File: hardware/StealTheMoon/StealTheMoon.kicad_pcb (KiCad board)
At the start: 2 copper layers, 21 parts, among them J1 Motor, J2 Motor, J3 Servo, J4 Servo, J5 Conn_01x10, J6 BAT, U1 ESP32-DEVKIT-V1, U2 ROB-14450, U3 L7805CV, U4 L7805CV

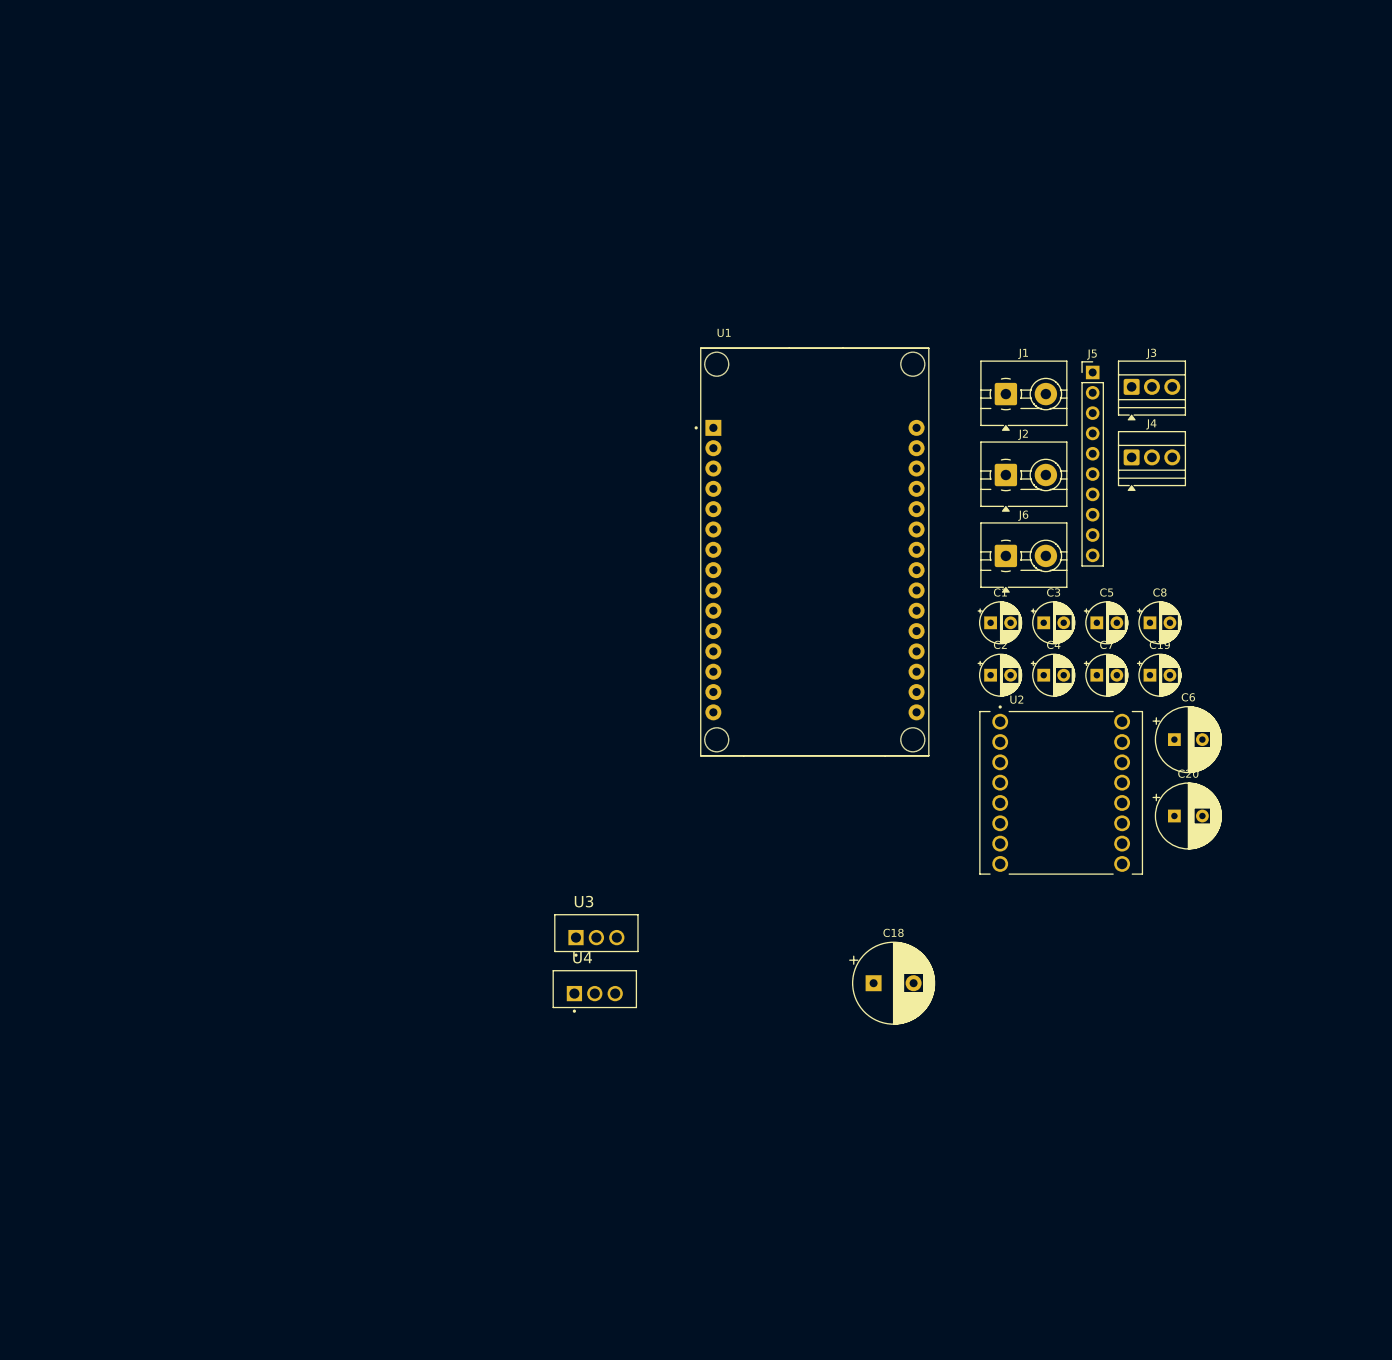
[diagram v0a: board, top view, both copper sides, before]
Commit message: Finish layout and generate gbr files for fabrication
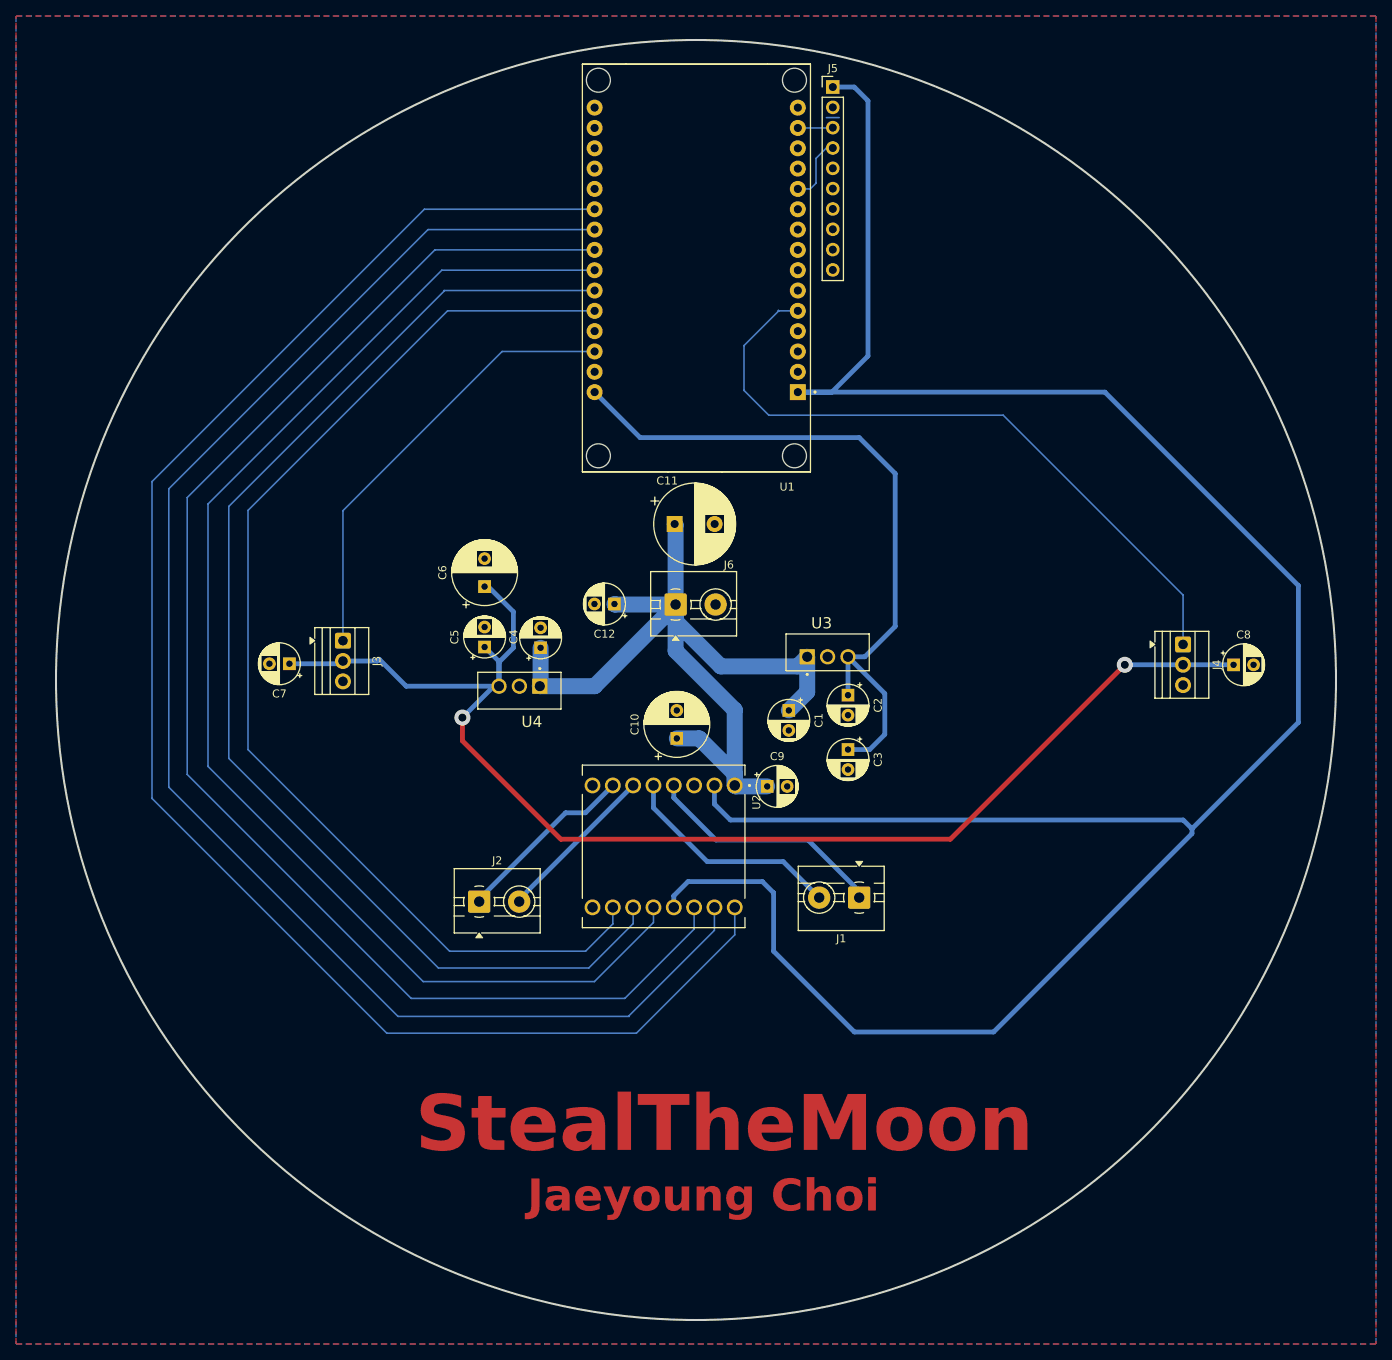
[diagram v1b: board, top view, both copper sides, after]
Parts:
- added C9: 100n, Capacitor_THT:CP_Radial_D5.0mm_P2.50mm, F.Cu at (112.9, 112.3)
- moved J3 103.6 mm to (59.9, 94.1), turned to -90 degrees
- moved C7 100.9 mm to (53.2, 97.0), turned to 180 degrees
- moved C6 88.3 mm to (77.6, 87.3), turned to 90 degrees
- moved J2 84.7 mm to (76.9, 126.7)
- moved C5 76.6 mm to (77.6, 94.9), turned to 90 degrees
- moved C12 67.5 mm to (93.8, 89.5), turned to 180 degrees
- moved J1 65.6 mm to (124.4, 126.2), turned to 180 degrees
- moved C4 63.0 mm to (84.6, 95.0), turned to 90 degrees
- moved C10 63.0 mm to (101.6, 106.3), turned to 90 degrees
- moved C11 62.6 mm to (101.3, 79.5)
- moved U2 50.1 mm to (100.0, 119.8), turned to -90 degrees
- moved J5 48.3 mm to (121.1, 24.9)
- moved U3 45.5 mm to (117.9, 96.1)
- moved J6 41.7 mm to (101.5, 89.6)
- moved U4 38.7 mm to (84.5, 99.8), turned to 180 degrees
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- renumbered C20 to C10, C18 to C11, C19 to C12
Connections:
- U1 pad 21: /PWMB -> /PWMA
- U1 pad 22: /BI1 -> /AI2
- U1 pad 23: /AI2 -> /AI1
- U1 pad 24: /AI1 -> /BI1
- U1 pad 25: /PWMA -> /BI2
- U1 pad 26: /BI2 -> /PWMB
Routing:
- net 3.3V: track 0.00 -> 309.3 mm
- net /PWMA: track 0.00 -> 202.6 mm
- net /AI2: track 0.00 -> 191.5 mm
- net /AI1: track 0.00 -> 179.6 mm
- net 5V2: track 0.00 -> 168.2 mm, vias 0 -> 2
- net /BI1: track 0.00 -> 165.0 mm
- net /BI2: track 0.00 -> 154.2 mm
- net /PWMB: track 0.00 -> 143.1 mm
- net 9V: track 0.00 -> 113.2 mm
- net 5V1: track 0.00 -> 90.8 mm
- net /Sv2: track 0.00 -> 85.9 mm
- net /Sv1: track 0.00 -> 56.0 mm
- net Net-(J1-Pin_1): track 0.00 -> 30.4 mm
- net Net-(J1-Pin_2): track 0.00 -> 28.2 mm
- net Net-(J2-Pin_1): track 0.00 -> 22.9 mm
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- added copper zone on B.Cu, net GND
- added copper zone on F.Cu, net GND
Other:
- board outline added: 160 x 160 mm
- copper layers 2 -> 4
- board text added: "Jaeyoung Choi"
- board text added: "StealTheMoon"

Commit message: Reroute the PCB to make it smaller
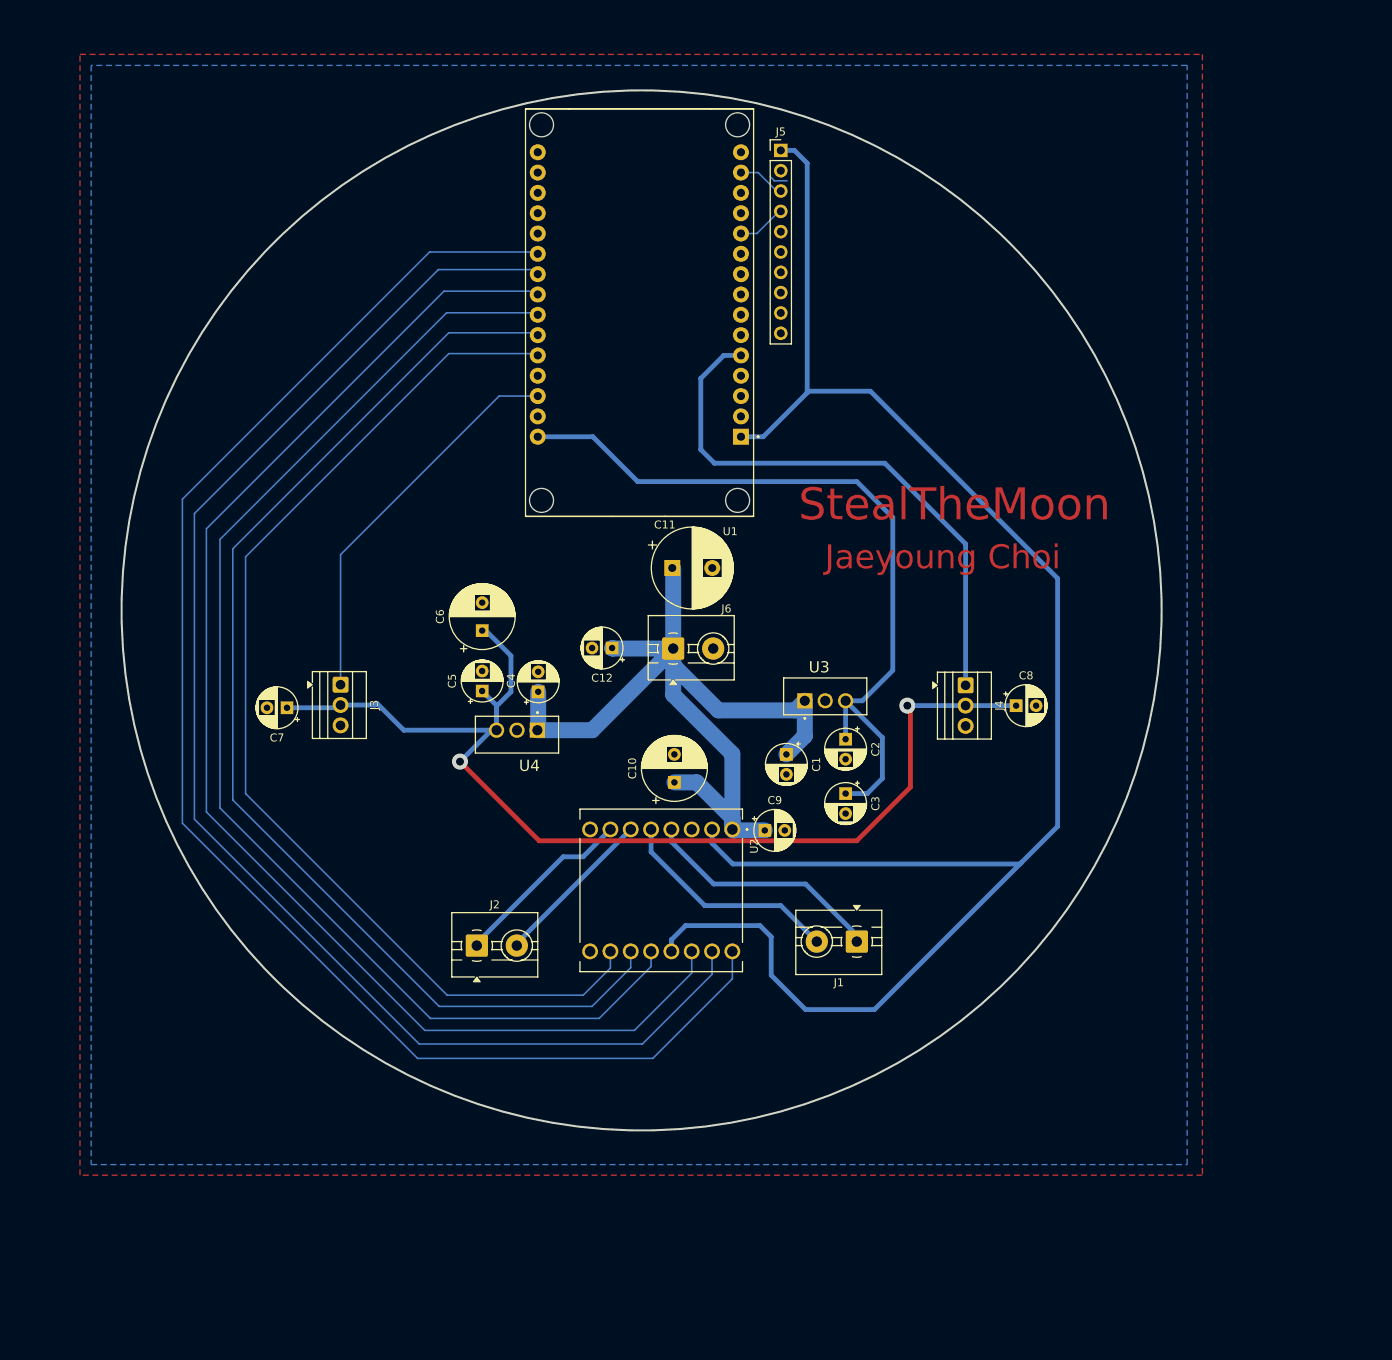
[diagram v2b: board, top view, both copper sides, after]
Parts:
- moved C8 27.7 mm to (144.0, 102.2)
- moved J4 27.7 mm to (137.7, 99.7)
- moved J5 10.2 mm to (114.6, 32.8)
- moved U1 9.03 mm to (96.9, 53.1)
- moved C12 5.51 mm to (93.5, 95.0)
- moved C9 5.51 mm to (112.6, 117.8)
- moved U3 5.51 mm to (117.6, 101.6)
- moved C1 5.51 mm to (115.3, 108.3)
- moved C10 5.51 mm to (101.3, 111.8)
- moved C11 5.51 mm to (101.0, 85.0)
- moved C2 5.51 mm to (122.7, 106.4)
- moved C3 5.51 mm to (122.7, 113.2)
- moved C4 5.51 mm to (84.3, 100.5)
- moved C5 5.51 mm to (77.3, 100.4)
- moved C6 5.51 mm to (77.3, 92.8)
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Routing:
- net 3.3V: track 309.3 -> 223.9 mm
- net 5V2: track 168.2 -> 141.9 mm
- net /PWMA: track 202.6 -> 186.3 mm
- net /Sv2: track 85.9 -> 70.8 mm
- net /AI2: track 191.5 -> 176.8 mm
- net /AI1: track 179.6 -> 166.9 mm
- net /BI1: track 165.0 -> 154.5 mm
- net /BI2: track 154.2 -> 145.3 mm
- net /Sv1: track 56.0 -> 49.1 mm
- net /PWMB: track 143.1 -> 136.3 mm
- net 5V1: track 90.8 -> 97.5 mm
- net /SDA: track 8.31 -> 6.13 mm
- net /SCL: track 4.39 -> 5.94 mm
- net GND: track 1.60 -> 2.31 mm
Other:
- board size 160 x 160 mm -> 130 x 130 mm
